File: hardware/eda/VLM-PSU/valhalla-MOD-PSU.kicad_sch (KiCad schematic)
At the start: 21 parts, among them J1 MAINS, J2 DC, J3 BUS, U1 *2

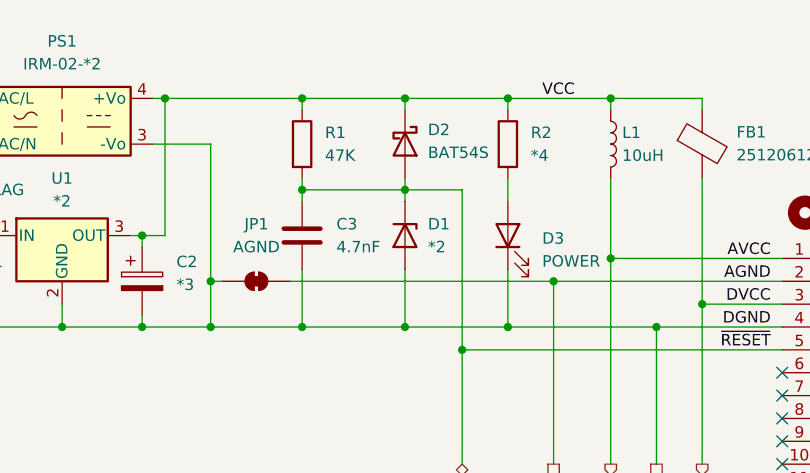
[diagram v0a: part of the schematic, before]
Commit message: UPDATE: formal dimensions for Valhalla MOD and progrss on CPU
 - added formal dimensions to the Valhalla MOD PSU PCB, to serve as a
   future template and as documentation
 - changed Zener/Schottky symbols to filled variant on same module,
   as customary in the EU
 - solved the Vio independence issue for the UI LEDs on the CPU module
   with a switchable regulator
 - finalized canonical dimensions of the CPU module and placed UI
   LEDs in two rows.
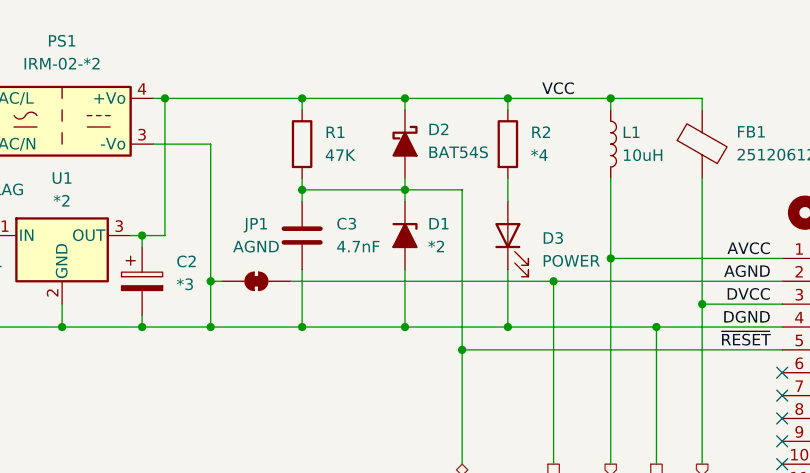
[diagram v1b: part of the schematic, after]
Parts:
- removed D1: *2, Diode_THT:D_DO-35_SOD27_P7.62mm_Horizontal, symbol Device:D_Zener
- removed D2: BAT54S, Diode_THT:D_DO-35_SOD27_P7.62mm_Horizontal, symbol Device:D_Schottky
- added D1: *2, Diode_THT:D_DO-35_SOD27_P7.62mm_Horizontal, symbol Device:D_Zener_Filled
- added D2: BAT54S, Diode_THT:D_DO-35_SOD27_P7.62mm_Horizontal, symbol Device:D_Schottky_Filled
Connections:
- net DGND: now also D1.2 (A)
- net VCC: now also D2.1 (K)
- net ~{RESET}: now also D1.1 (K), D2.2 (A)
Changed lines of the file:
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@@
 	(label "AVCC"
 		(at 161.29 41.91 180)
-		(fields_autoplaced yes)
 		(effects
 			(font
@@
 	(label "AGND"
 		(at 161.29 44.45 180)
-		(fields_autoplaced yes)
 		(effects
 			(font
@@
 	(label "DVCC"
 		(at 161.29 46.99 180)
-		(fields_autoplaced yes)
 		(effects
 			(font
@@
 	(label "~{RESET}"
 		(at 161.29 52.07 180)
-		(fields_autoplaced yes)
 		(effects
 			(font
@@
 	(label "DGND"
 		(at 161.29 49.53 180)
-		(fields_autoplaced yes)
 		(effects
 			(font
@@
 	(label "VCC"
 		(at 135.89 24.13 0)
-		(fields_autoplaced yes)
 		(effects
 			(font
@@
 		(shape passive)
 		(at 148.59 64.77 270)
-		(fields_autoplaced yes)
 		(effects
 			(font
@@
 		(shape output)
 		(at 143.51 64.77 270)
-		(fields_autoplaced yes)
 		(effects
 			(font
@@
 		(shape output)
 		(at 153.67 64.77 270)
-		(fields_autoplaced yes)
 		(effects
 			(font
@@
 		(shape passive)
 		(at 137.16 64.77 270)
-		(fields_autoplaced yes)
 		(effects
 			(font
@@
 		(shape bidirectional)
 		(at 127 64.77 270)
-		(fields_autoplaced yes)
 		(effects
 			(font
@@
 				)
 				(justify left)
-			)
-		)
-	)
-	(symbol
-		(lib_id "Device:D_Zener")
-		(at 120.65 39.37 270)
-		(unit 1)
-		(exclude_from_sim no)
-		(in_bom yes)
-		(on_board yes)
-		(dnp no)
-		(fields_autoplaced yes)
-		(property "Reference" "D1"
-			(at 123.19 38.0999 90)
-			(effects
-				(font
-					(size 1.27 1.27)
-				)
-				(justify left)
-			)
-		)
-		(property "Value" "*2"
-			(at 123.19 40.6399 90)
-			(effects
-				(font
-					(size 1.27 1.27)
-				)
-				(justify left)
-			)
-		)
-		(property "Footprint" "Diode_THT:D_DO-35_SOD27_P7.62mm_Horizontal"
-			(at 120.65 39.37 0)
-			(effects
-				(font
-					(size 1.27 1.27)
-				)
-				(hide yes)
-			)
-		)
-		(property "Datasheet" "~"
-			(at 120.65 39.37 0)
-			(effects
-				(font
-					(size 1.27 1.27)
-				)
-				(hide yes)
-			)
-		)
-		(property "Description" "Zener diode"
-			(at 120.65 39.37 0)
-			(effects
-				(font
-					(size 1.27 1.27)
-				)
-				(hide yes)
-			)
-		)
-		(pin "1"
-		)
-		(pin "2"
-		)
-		(instances
-			(project ""
-				(path "/679144a0-43a8-4e3b-bec8-ba1ed1e1bb89"
-					(reference "D1")
-					(unit 1)
-				)
 			)
 		)
@@
 	)
 	(symbol
+		(lib_id "Device:D_Zener_Filled")
+		(at 120.65 39.37 270)
+		(unit 1)
+		(exclude_from_sim no)
+		(in_bom yes)
+		(on_board yes)
+		(dnp no)
+		(fields_autoplaced yes)
+		(property "Reference" "D1"
+			(at 123.19 38.0999 90)
+			(effects
+				(font
+					(size 1.27 1.27)
+				)
+				(justify left)
+			)
+		)
+		(property "Value" "*2"
+			(at 123.19 40.6399 90)
+			(effects
+				(font
+					(size 1.27 1.27)
+				)
+				(justify left)
+			)
+		)
+		(property "Footprint" "Diode_THT:D_DO-35_SOD27_P7.62mm_Horizontal"
+			(at 120.65 39.37 0)
+			(effects
+				(font
+					(size 1.27 1.27)
+				)
+				(hide yes)
+			)
+		)
+		(property "Datasheet" "~"
+			(at 120.65 39.37 0)
+			(effects
+				(font
+					(size 1.27 1.27)
+				)
+				(hide yes)
+			)
+		)
+		(property "Description" "Zener diode, filled shape"
+			(at 120.65 39.37 0)
+			(effects
+				(font
+					(size 1.27 1.27)
+				)
+				(hide yes)
+			)
+		)
+		(pin "1"
+		)
+		(pin "2"
+		)
+		(instances
+			(project ""
+				(path "/679144a0-43a8-4e3b-bec8-ba1ed1e1bb89"
+					(reference "D1")
+					(unit 1)
+				)
+			)
+		)
+	)
+	(symbol
 		(lib_id "Device:Fuse")
 		(at 57.15 24.13 90)
@@
 	)
 	(symbol
-		(lib_id "Device:D_Schottky")
+		(lib_id "Device:D_Schottky_Filled")
 		(at 120.65 29.21 270)
 		(unit 1)
@@
 			)
 		)
-		(property "Description" "Schottky diode"
+		(property "Description" "Schottky diode, filled shape"
 			(at 120.65 29.21 0)
 			(effects

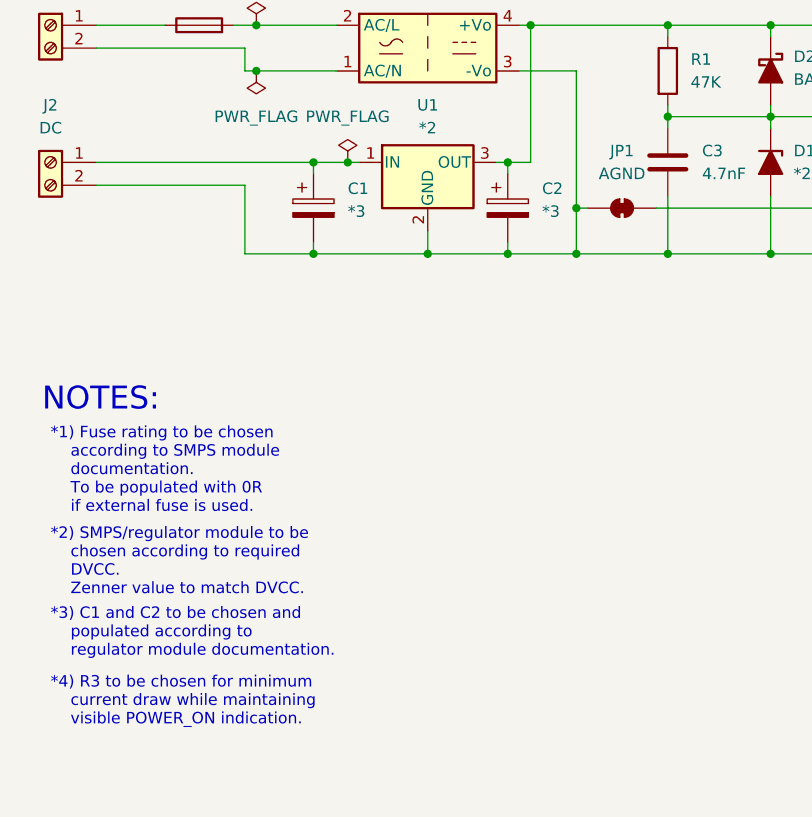
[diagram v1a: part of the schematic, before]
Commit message: UPDATE: progress towards templatizing dimensions   - used the PSU module as a master copy for now until the template     stabilizes, to be exported as a stand-alone blueprint for future     modules   - minor progress on the CPU(ATMega) module: easier to solder     footprint for LVCC regulator, crystal dress-up and reference     clean-ups.
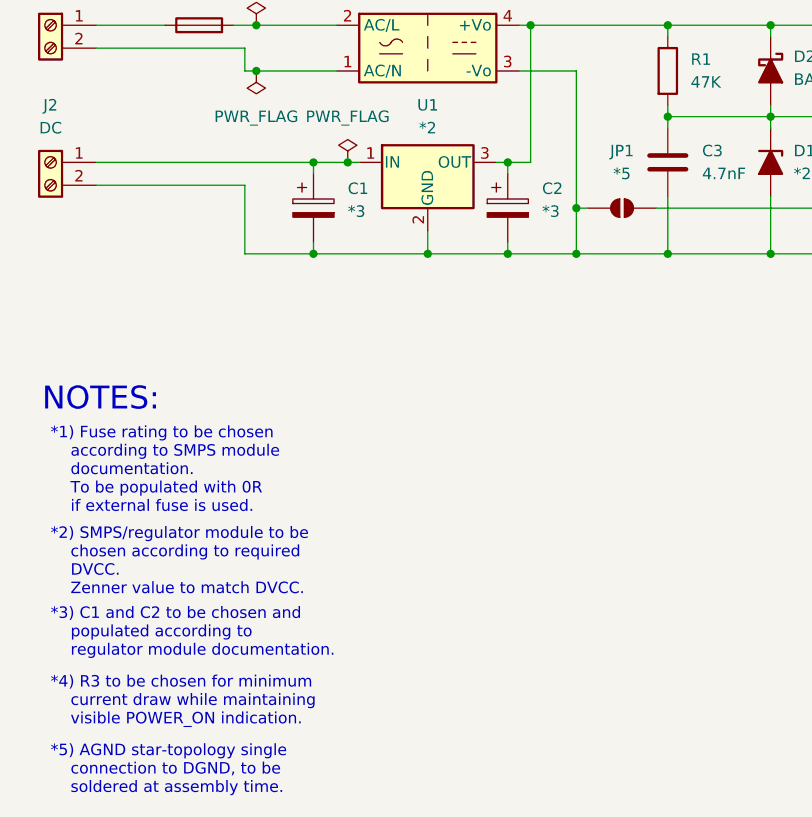
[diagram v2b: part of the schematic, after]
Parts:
- removed JP1: AGND, Jumper:SolderJumper-2_P1.3mm_Bridged2Bar_RoundedPad1.0x1.5mm, symbol Jumper:SolderJumper_2_Bridged
- added JP1: *5, Jumper:SolderJumper-2_P1.3mm_Open_RoundedPad1.0x1.5mm, symbol Jumper:SolderJumper_2_Open
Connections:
- net AGND: now also JP1.2 (B)
- net DGND: now also JP1.1 (A)
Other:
- note added: "*5) AGND star-topology single connection to DGND, to be soldered at assembly time."
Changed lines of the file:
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@@
+		)
+	)
+	(text "*5) AGND star-topology single\n    connection to DGND, to be\n    soldered at assembly time."
+		(exclude_from_sim no)
+		(at 40.64 106.934 0)
+		(effects
+			(font
+				(size 1.27 1.27)
+			)
+			(justify left)
 		)
 	)
@@
 	)
 	(symbol
-		(lib_id "Jumper:SolderJumper_2_Bridged")
-		(at 104.14 44.45 180)
+		(lib_id "Device:FerriteBead")
+		(at 153.67 29.21 0)
+		(unit 1)
+		(exclude_from_sim no)
+		(in_bom yes)
+		(on_board yes)
+		(dnp no)
+		(fields_autoplaced yes)
+		(property "Reference" "FB1"
+			(at 157.48 27.8891 0)
+			(effects
+				(font
+					(size 1.27 1.27)
+				)
+				(justify left)
+			)
+		)
+		(property "Value" "2512061217Y0"
+			(at 157.48 30.4291 0)
+			(effects
+				(font
+					(size 1.27 1.27)
+				)
+				(justify left)
+			)
+		)
+		(property "Footprint" "Inductor_THT:L_Axial_L5.0mm_D3.6mm_P10.00mm_Horizontal_Murata_BL01RN1A2A2"
+			(at 151.892 29.21 90)
+			(effects
+				(font
+					(size 1.27 1.27)
+				)
+				(hide yes)
+			)
+		)
+		(property "Datasheet" "~"
+			(at 153.67 29.21 0)
+			(effects
+				(font
+					(size 1.27 1.27)
+				)
+				(hide yes)
+			)
+		)
+		(property "Description" "Ferrite bead"
+			(at 153.67 29.21 0)
+			(effects
+				(font
+					(size 1.27 1.27)
+				)
+				(hide yes)
+			)
+		)
+		(pin "1"
+		)
+		(pin "2"
+		)
+		(instances
+			(project ""
+				(path "/679144a0-43a8-4e3b-bec8-ba1ed1e1bb89"
+					(reference "FB1")
+					(unit 1)
+				)
+			)
+		)
+	)
+	(symbol
+		(lib_id "Jumper:SolderJumper_2_Open")
+		(at 104.14 44.45 0)
 		(unit 1)
 		(exclude_from_sim yes)
@@
 			)
 		)
-		(property "Value" "AGND"
+		(property "Value" "*5"
 			(at 104.14 40.64 0)
 			(effects
@@
 			)
 		)
-		(property "Footprint" "Jumper:SolderJumper-2_P1.3mm_Bridged2Bar_RoundedPad1.0x1.5mm"
+		(property "Footprint" "Jumper:SolderJumper-2_P1.3mm_Open_RoundedPad1.0x1.5mm"
 			(at 104.14 44.45 0)
 			(effects
@@
 			)
 		)
-		(property "Description" "Solder Jumper, 2-pole, closed/bridged"
+		(property "Description" "Solder Jumper, 2-pole, open"
 			(at 104.14 44.45 0)
 			(effects
@@
 					(unit 1)
 				)
-			)
-		)
-	)
-	(symbol
-		(lib_id "Device:FerriteBead")
-		(at 153.67 29.21 0)
-		(unit 1)
-		(exclude_from_sim no)
-		(in_bom yes)
-		(on_board yes)
-		(dnp no)
-		(fields_autoplaced yes)
-		(property "Reference" "FB1"
-			(at 157.48 27.8891 0)
-			(effects
-				(font
-					(size 1.27 1.27)
-				)
-				(justify left)
-			)
-		)
-		(property "Value" "2512061217Y0"
-			(at 157.48 30.4291 0)
-			(effects
-				(font
-					(size 1.27 1.27)
-				)
-				(justify left)
-			)
-		)
-		(property "Footprint" "Inductor_THT:L_Axial_L5.0mm_D3.6mm_P10.00mm_Horizontal_Murata_BL01RN1A2A2"
-			(at 151.892 29.21 90)
-			(effects
-				(font
-					(size 1.27 1.27)
-				)
-				(hide yes)
-			)
-		)
-		(property "Datasheet" "~"
-			(at 153.67 29.21 0)
-			(effects
-				(font
-					(size 1.27 1.27)
-				)
-				(hide yes)
-			)
-		)
-		(property "Description" "Ferrite bead"
-			(at 153.67 29.21 0)
-			(effects
-				(font
-					(size 1.27 1.27)
-				)
-				(hide yes)
-			)
-		)
-		(pin "1"
-		)
-		(pin "2"
-		)
-		(instances
-			(project ""
-				(path "/679144a0-43a8-4e3b-bec8-ba1ed1e1bb89"
-					(reference "FB1")
-					(unit 1)
-				)

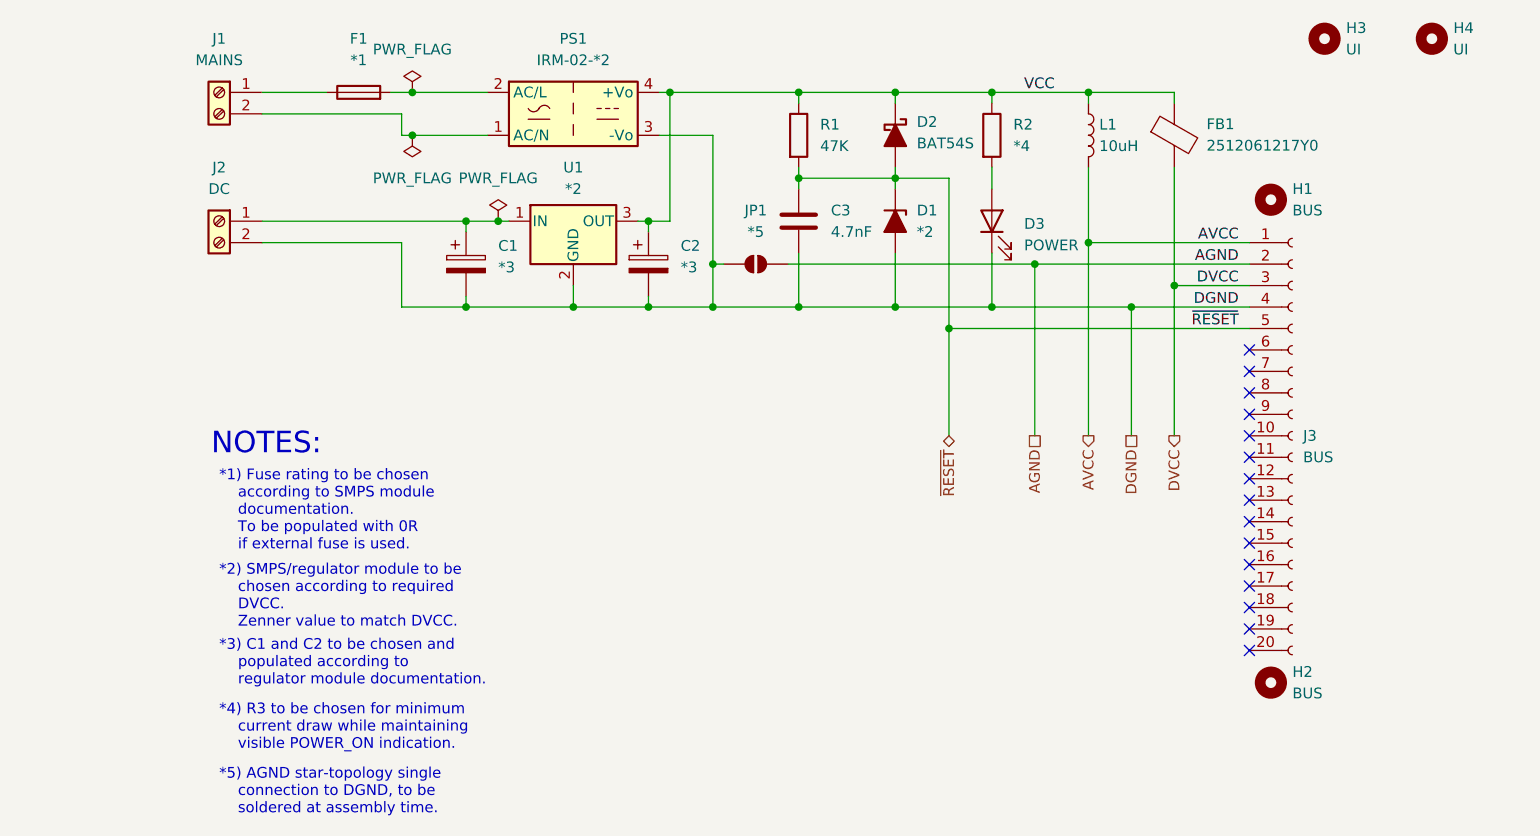
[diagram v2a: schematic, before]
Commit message: UPDATE: re-touched PSU after latest specification release
  - added LVCC and BVCC and polyfuses on all outputs
  - added simple LVCC control via GPIO
  - layout update to follow.
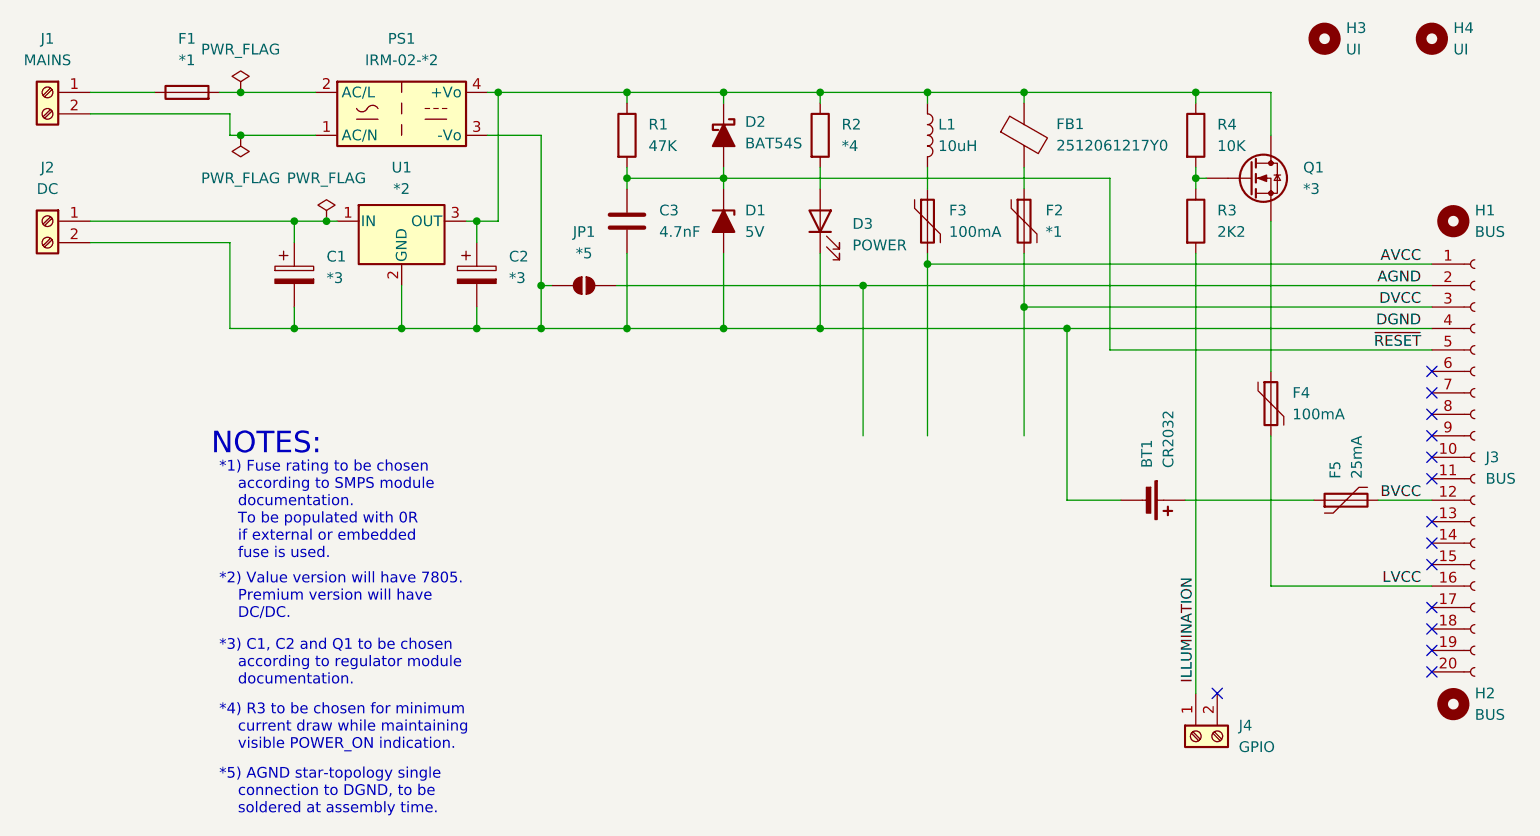
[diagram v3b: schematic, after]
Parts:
- added BT1: CR2032, Battery:Battery_Panasonic_CR2032-VS1N_Vertical_CircularHoles, symbol Device:Battery_Cell
- added F2: *1, Fuse:Fuse_BelFuse_0ZRE0005FF_L8.3mm_W3.8mm, symbol Device:Polyfuse
- added F3, F4: 100mA, Fuse:Fuse_BelFuse_0ZRE0005FF_L8.3mm_W3.8mm, symbol Device:Polyfuse
- added F5: 25mA, Fuse:Fuse_BelFuse_0ZRE0005FF_L8.3mm_W3.8mm, symbol Device:Polyfuse
- added J4: GPIO, TerminalBlock_Phoenix:TerminalBlock_Phoenix_MPT-0,5-2-2.54_1x02_P2.54mm_Horizontal, symbol Connector:Screw_Terminal_01x02
- added Q1: *3, Package_TO_SOT_THT:TO-92, symbol Device:Q_NMOS
- added R3: 2K2, Resistor_THT:R_Axial_DIN0207_L6.3mm_D2.5mm_P7.62mm_Horizontal, symbol Device:R
- added R4: 10K, Resistor_THT:R_Axial_DIN0207_L6.3mm_D2.5mm_P7.62mm_Horizontal, symbol Device:R
- D1: value *2 -> 5V
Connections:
- net AVCC: now also F3.2; no longer L1.2
- net DGND: now also BT1.2 (-)
- net DVCC: now also F2.2; no longer FB1.2
- net BVCC: now reaches J3.12 (Pin_12)
- net BVCC: now also F5.2
- net LVCC: now reaches J3.16 (Pin_16)
- net LVCC: now also F4.2
- net VCC: no longer names the net of C2.1, D2.1 (K), FB1.1, L1.1, PS1.4 (+Vo), R1.1, R2.1, U1.3 (OUT)
- net VCC: now also Q1.D, R4.1
- new net: F3.1, L1.2
- new net: BT1.1 (+), F5.1
- new net: F2.1, FB1.2
- new net: F4.1, Q1.S
- new net: Q1.G, R3.1, R4.2
- new net ILLUMINATION: J4.1 (Pin_1), R3.2
- no-connect marks 15 -> 14
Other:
- note added: "*1) Fuse rating to be chosen according to SMPS module documentation. To be populated with 0R if external or embedded fuse is used."
- note added: "*2) Value version will have 7805. Premium version will have DC/DC."
- note added: "*3) C1, C2 and Q1 to be chosen according to regulator module documentation."
- note removed: "*1) Fuse rating to be chosen according to SMPS module documentation. To be populated with 0R if external fuse is used."
- note removed: "*2) SMPS/regulator module to be chosen according to required DVCC. Zenner value to match DVCC."
- note removed: "*3) C1 and C2 to be chosen and populated according to regulator module documentation."
- moved on the sheet: C1, C2, C3, D1, D2, D3, F1, FB1, H1, H2, J1, J2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

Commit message: UPDATE: MOD-PSU re-layout complete, RTM.
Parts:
- removed Q1: *3, Package_TO_SOT_THT:TO-92, symbol Device:Q_NMOS
- added D4: BAT54, Diode_THT:D_DO-35_SOD27_P7.62mm_Horizontal, symbol Device:D_Schottky_Filled
- added Q1: *3, Package_TO_SOT_THT:TO-92_Inline, symbol Transistor_FET:BS170
- F4: value 100mA -> *3
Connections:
- net at F5.1: now also D4.1 (K); no longer BT1.1 (+)
- net at C2.1, D2.1 (K), FB1.1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: now also Q1.1 (D)
- net at F4.1: now also Q1.3 (S)
- net at R3.1, R4.2: now also Q1.2 (G)
- new net: BT1.1 (+), D4.2 (A)
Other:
- note added: "*1) F1 and F2 to be chosen according to SMPS module documentation. To be populated with 0R if external or embedded fuse is used."
- note added: "*3) C1, C2, Q1 and F4 to be chosen according to regulator module documentation. Value version will populate Q1 with 0R (S-D) and not populate R4 and R3."
- note removed: "*1) Fuse rating to be chosen according to SMPS module documentation. To be populated with 0R if external or embedded fuse is used."
- note removed: "*3) C1, C2 and Q1 to be chosen according to regulator module documentation."
- moved on the sheet: BT1, D2, F1, FB1, J1, L1, PS1, R1, R2, R3, R4

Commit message: UPDATE: cosmetic fixes to schematic defaults
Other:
- title: Valhalla MOD PSU Module -> Valhalla MOD-PSU
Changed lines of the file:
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@@
 	(paper "A5")
 	(title_block
-		(title "Valhalla MOD PSU Module")
-		(date "2025-01-04")
-		(rev "1")
+		(title "Valhalla MOD-PSU")
+		(date "2025-03-25")
+		(rev "2")
 	)
 	(text "NOTES:"
